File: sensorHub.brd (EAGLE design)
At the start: 160 x 100 mm, 11 parts

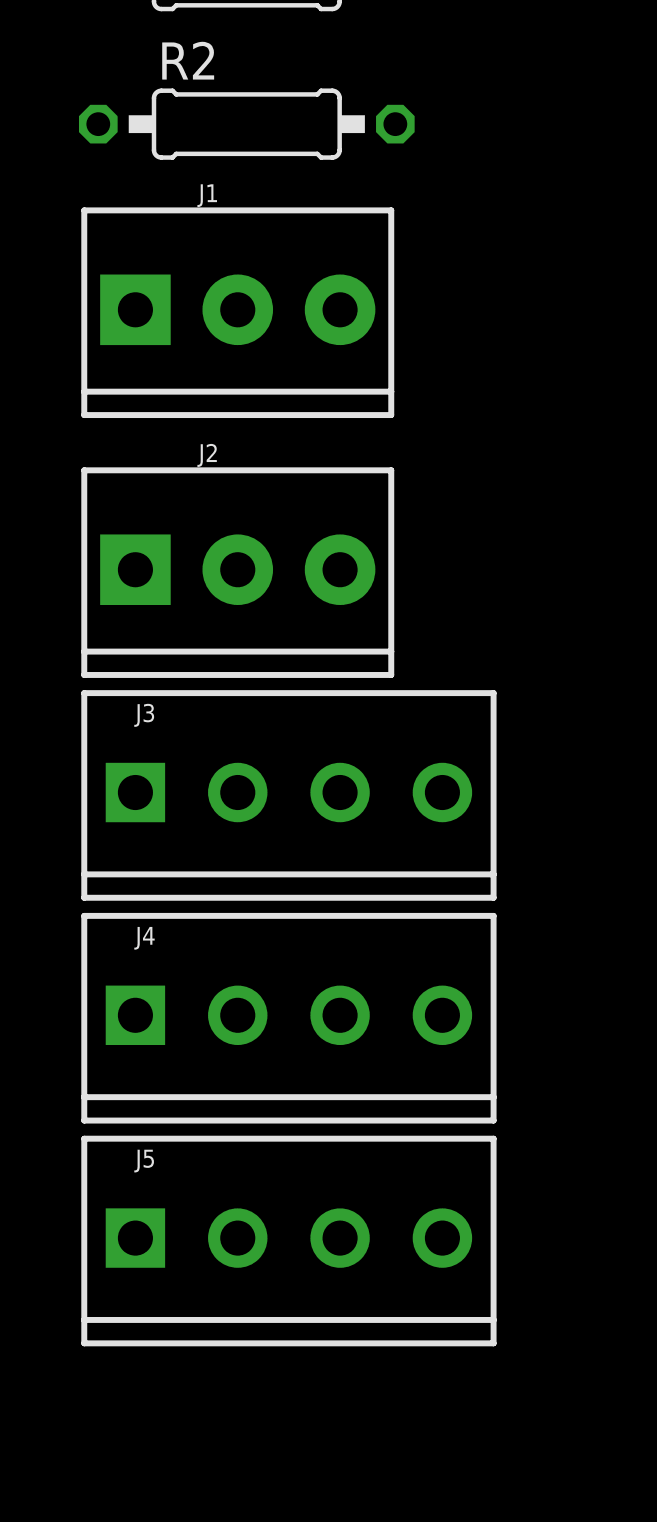
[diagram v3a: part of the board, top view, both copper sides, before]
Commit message: Completes connections in the schematic
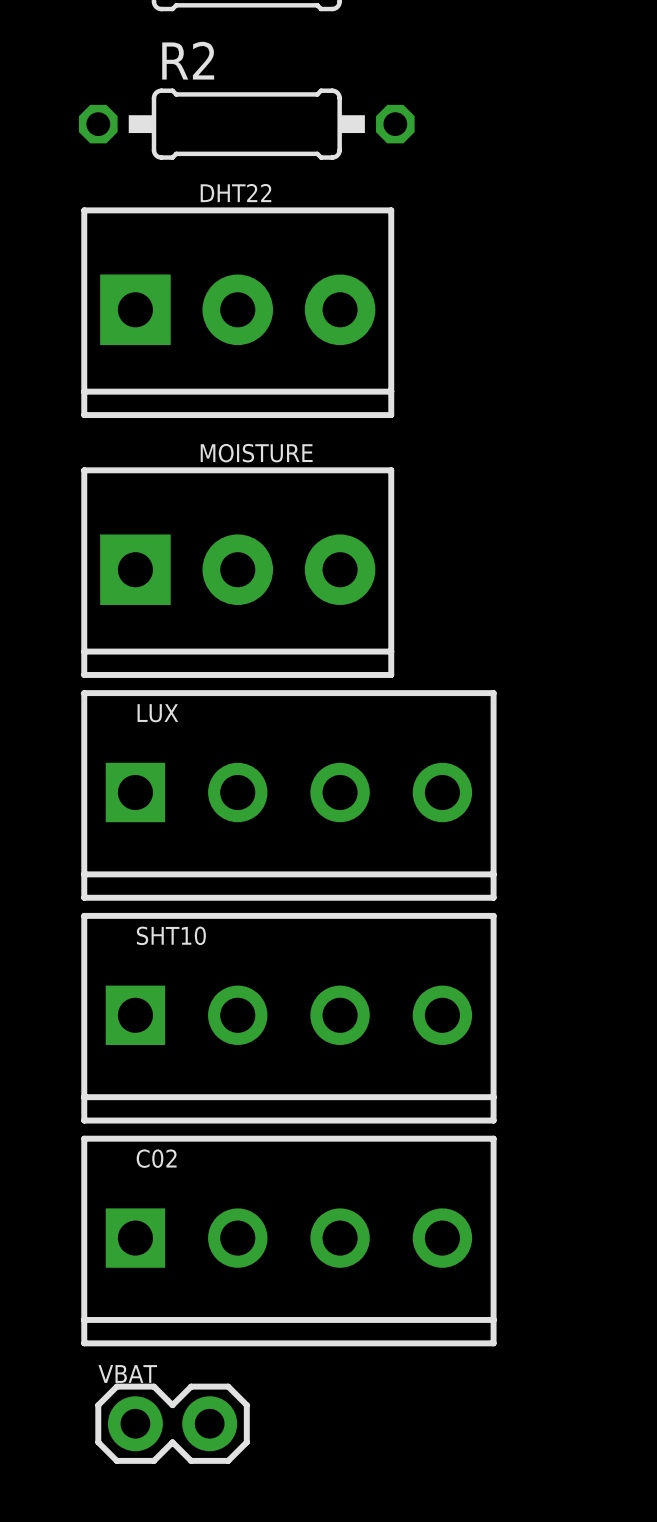
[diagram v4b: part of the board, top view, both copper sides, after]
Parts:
- added VBAT: (no value), SparkFun-Connectors:1X02
- R1, R2: value (none) -> 10k
- renumbered J1 to DHT22, J2 to MOISTURE, J3 to LUX, J4 to SHT10, J5 to C02
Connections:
- removed net OUT+: VR1.OUT+
- removed net OUT-: VR1.OUT-
- removed net VIN+: VR1.VIN+
- removed net VIN-: VR1.VIN-
- new net 3V: DHT22.1, JP1.3, JP1.4, LUX.1, MOISTURE.1, R1.1, R2.1, SHT10.1
- new net 5V: C02.2, VR1.OUT+
- new net A2: JP1.13, JP1.14, MOISTURE.2
- new net D5: DHT22.2, JP2.17, JP2.18
- new net N$1: JP1.1, JP1.2
- new net N$10: JP1.19, JP1.20
- new net N$11: JP1.21, JP1.22
- new net N$12: JP1.23, JP1.24
- new net N$13: JP1.25, JP1.26
- new net N$16: JP1.31, JP1.32
- new net N$17: JP2.1, JP2.2
- new net N$18: JP2.3, JP2.4
- new net N$19: JP2.5, JP2.6
- new net N$20: JP2.7, JP2.8
- new net N$21: JP2.10, JP2.9
- new net N$22: JP2.11, JP2.12
- new net N$23: JP2.13, JP2.14
- new net N$24: JP2.15, JP2.16
- new net N$27: VBAT.1, VBAT.2, VR1.VIN+
- new net N$3: JP1.5, JP1.6
- new net N$5: JP1.10, JP1.9
- new net N$6: JP1.11, JP1.12
- new net N$8: JP1.15, JP1.16
- new net N$9: JP1.17, JP1.18
- new net RX: C02.4, JP1.27, JP1.28
- new net SCL: JP2.19, JP2.20, LUX.3, R1.2, SHT10.3
- new net SDA: JP2.21, JP2.22, LUX.4, R2.2, SHT10.4
- new net TX: C02.3, JP1.29, JP1.30
- net GND: now also C02.1, DHT22.3, JP1.7, JP1.8, LUX.2, MOISTURE.3, SHT10.2, VR1.OUT-, VR1.VIN-

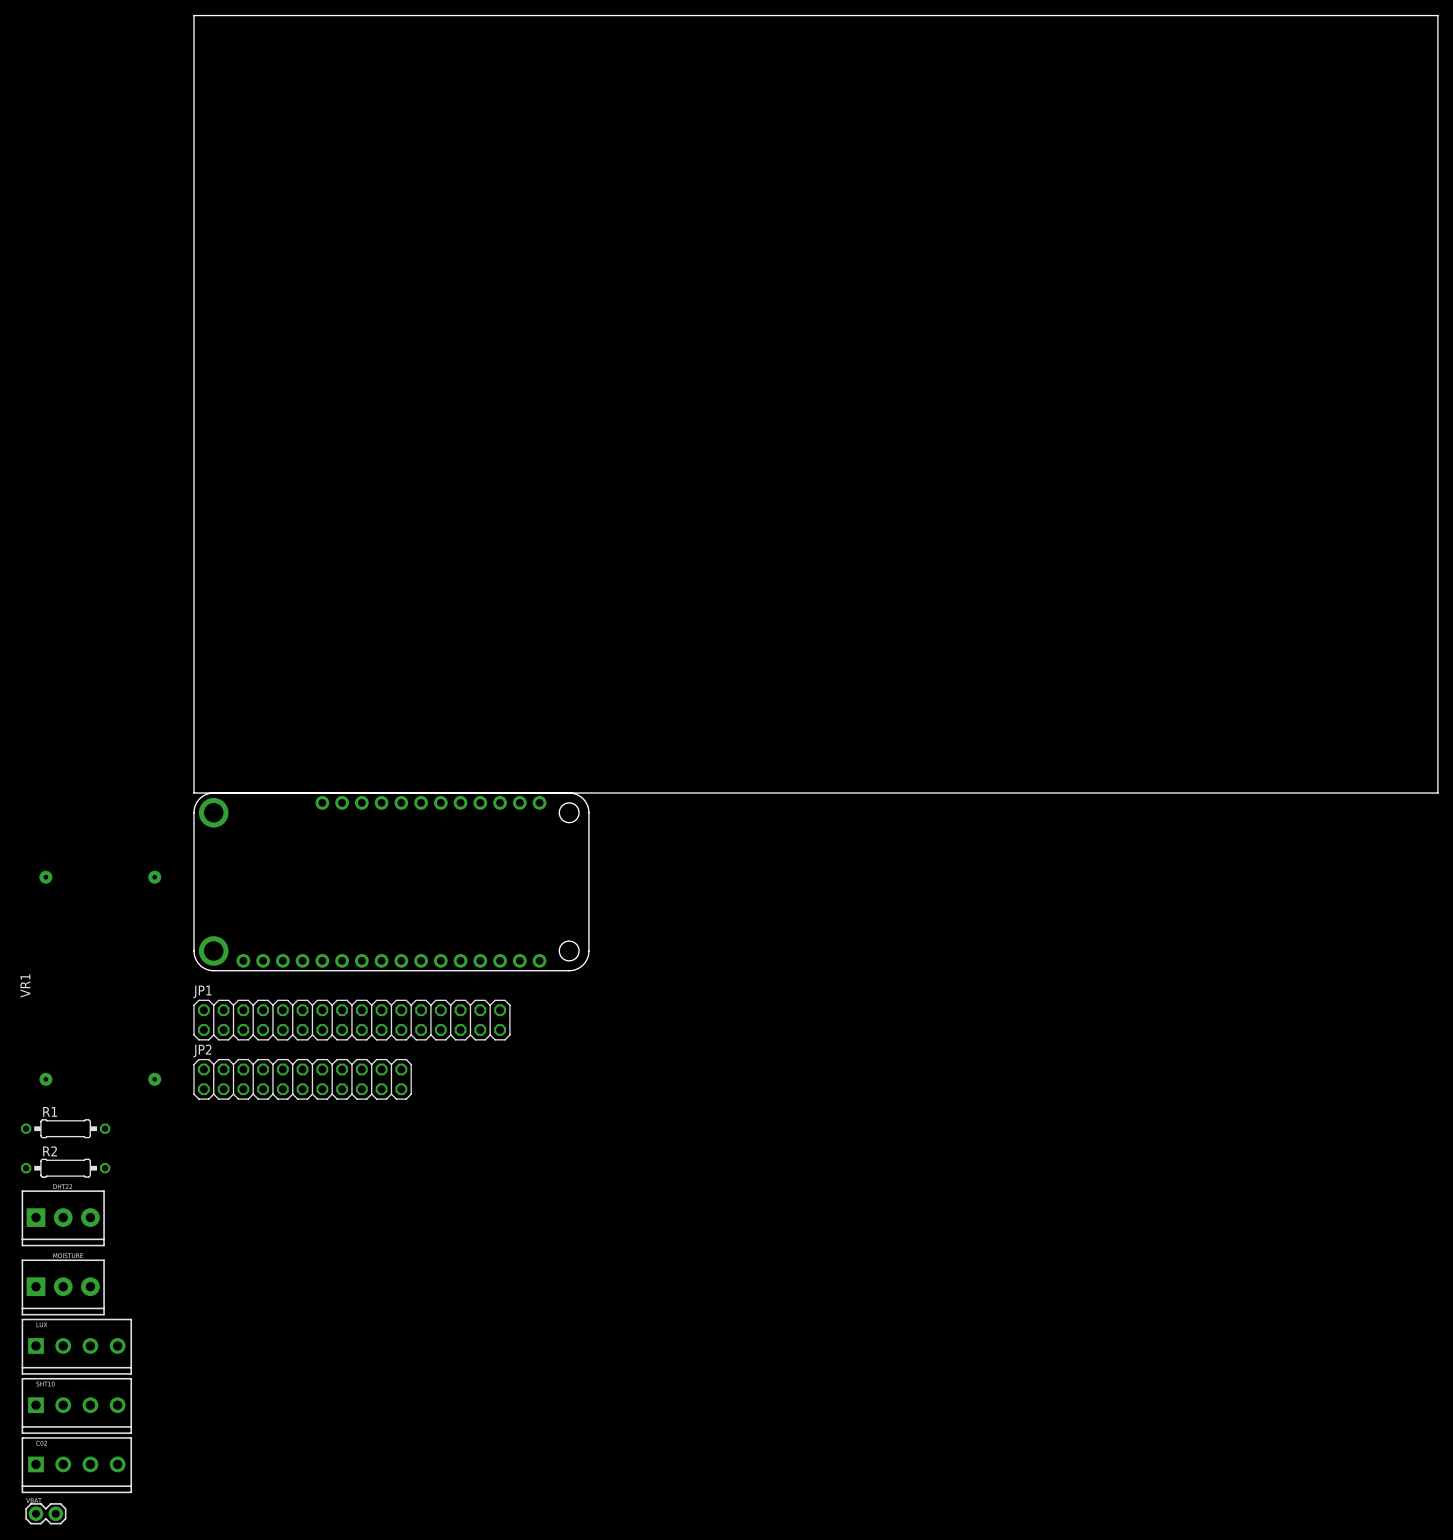
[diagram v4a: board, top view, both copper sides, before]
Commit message: Places components in pcb brd layout
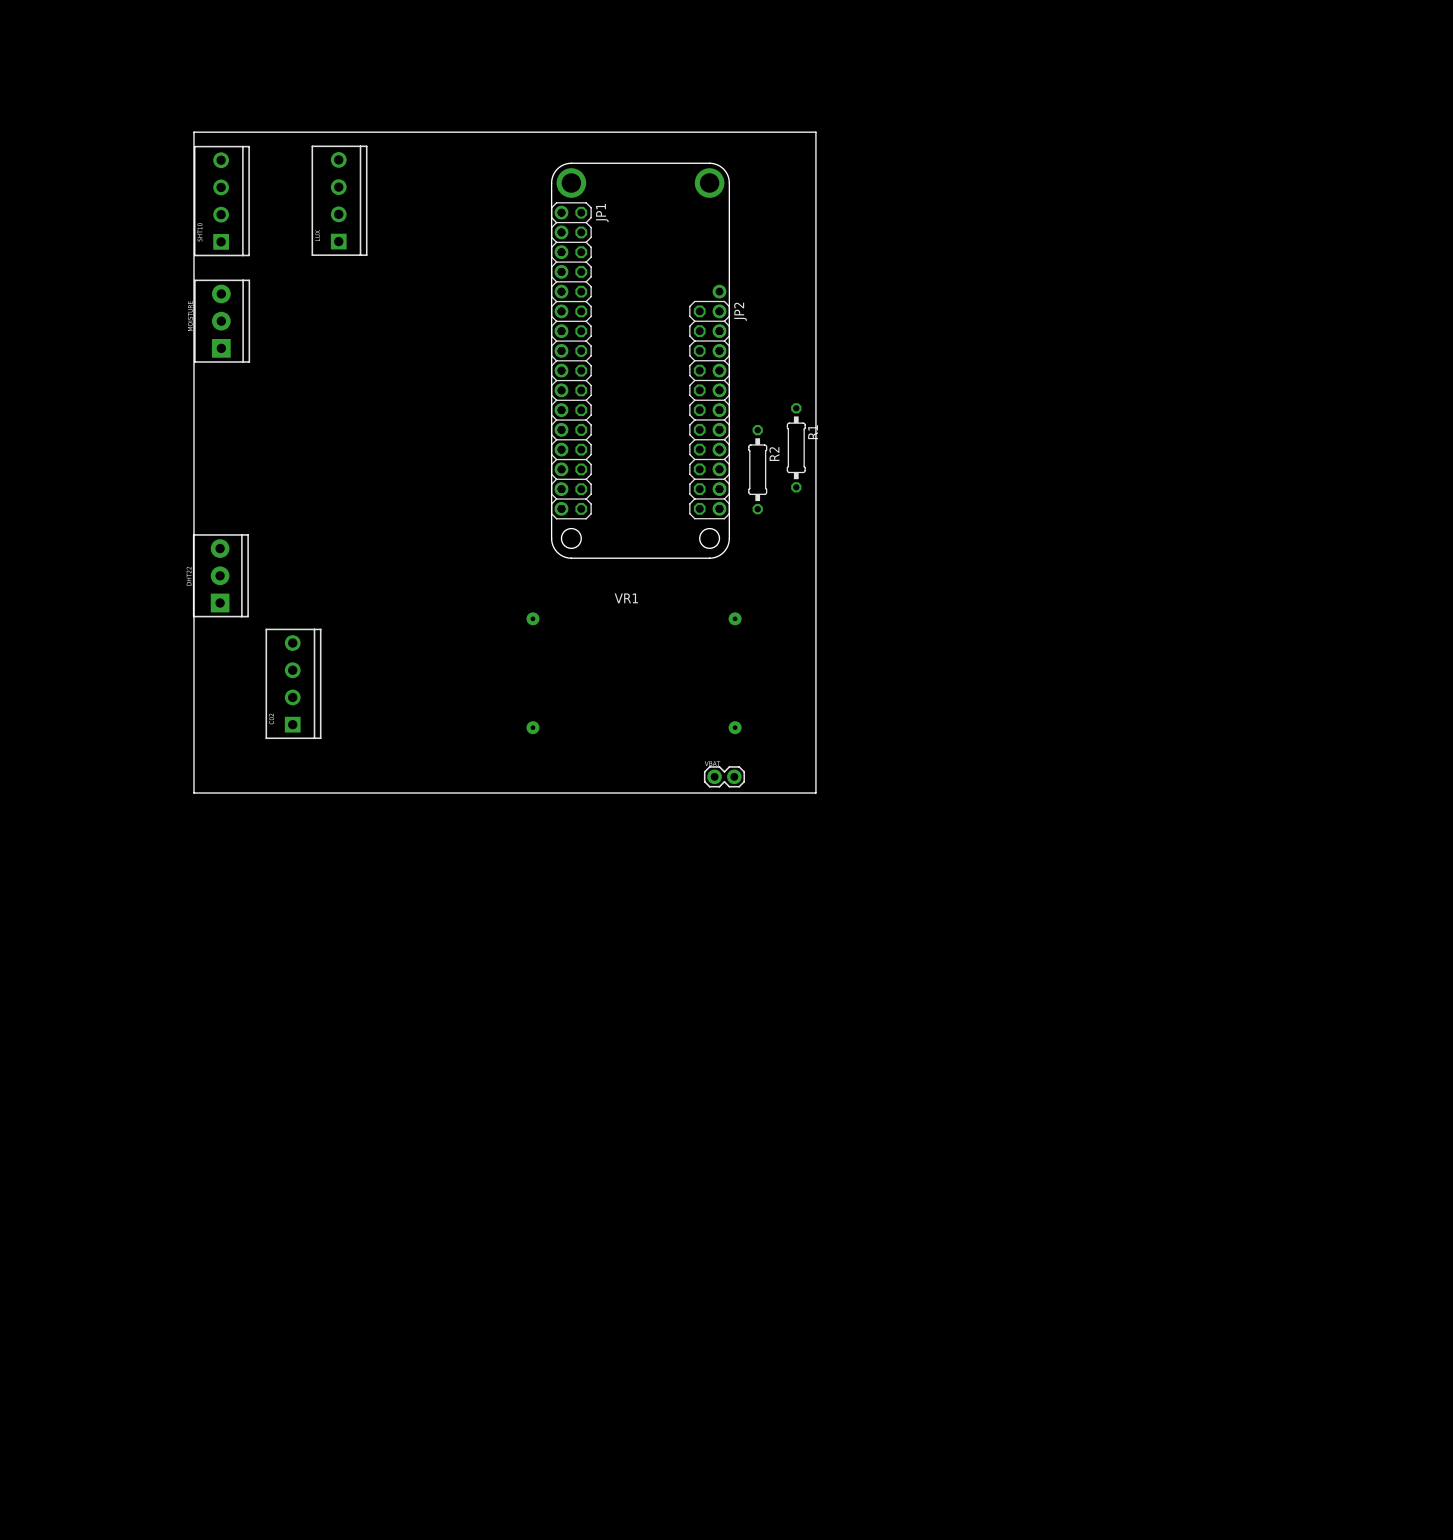
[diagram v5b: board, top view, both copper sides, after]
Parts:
- moved SHT10 151.5 mm to (3.49, 70.9), turned to 90 degrees
- moved LUX 147.3 mm to (18.6, 70.9), turned to 90 degrees
- moved VBAT 128.9 mm to (67.0, 2.08)
- moved R1 128.5 mm to (77.5, 44.4), turned to 270 degrees
- moved R2 126.5 mm to (72.5, 41.6), turned to 270 degrees
- moved MOISTURE 123.0 mm to (3.52, 57.2), turned to 90 degrees
- moved MS1 113.6 mm to (46.0, 81.0), turned to 270 degrees
- moved JP2 100.7 mm to (66.3, 49.2), turned to 270 degrees
- moved C02 100.7 mm to (12.7, 8.79), turned to 90 degrees
- moved JP1 89.4 mm to (48.5, 55.6), turned to 270 degrees
- moved VR1 86.2 mm to (43.6, 22.4), turned to 270 degrees
- moved DHT22 82.5 mm to (3.36, 24.4), turned to 90 degrees
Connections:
- net N$27 renamed VBAT
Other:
- board size 160 x 100 mm -> 80 x 85 mm

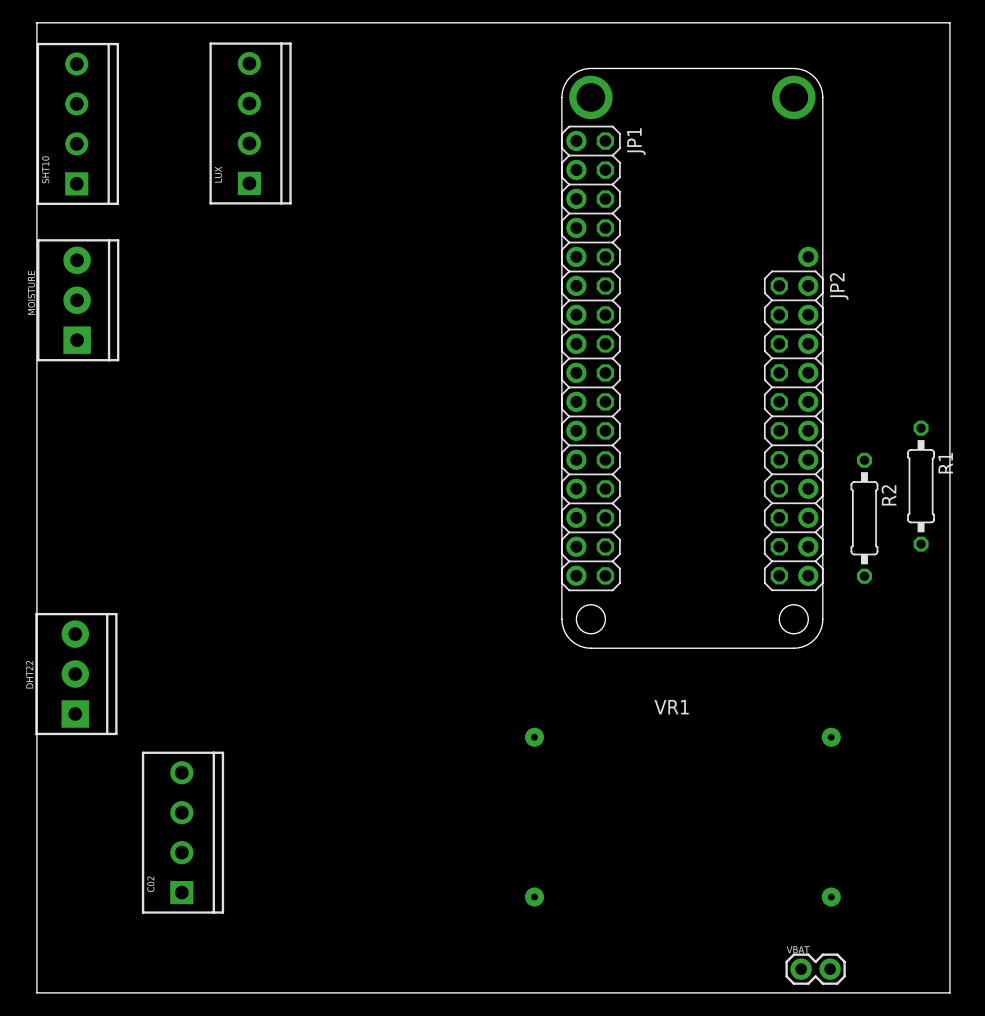
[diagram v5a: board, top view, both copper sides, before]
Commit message: Set components in place in brd file
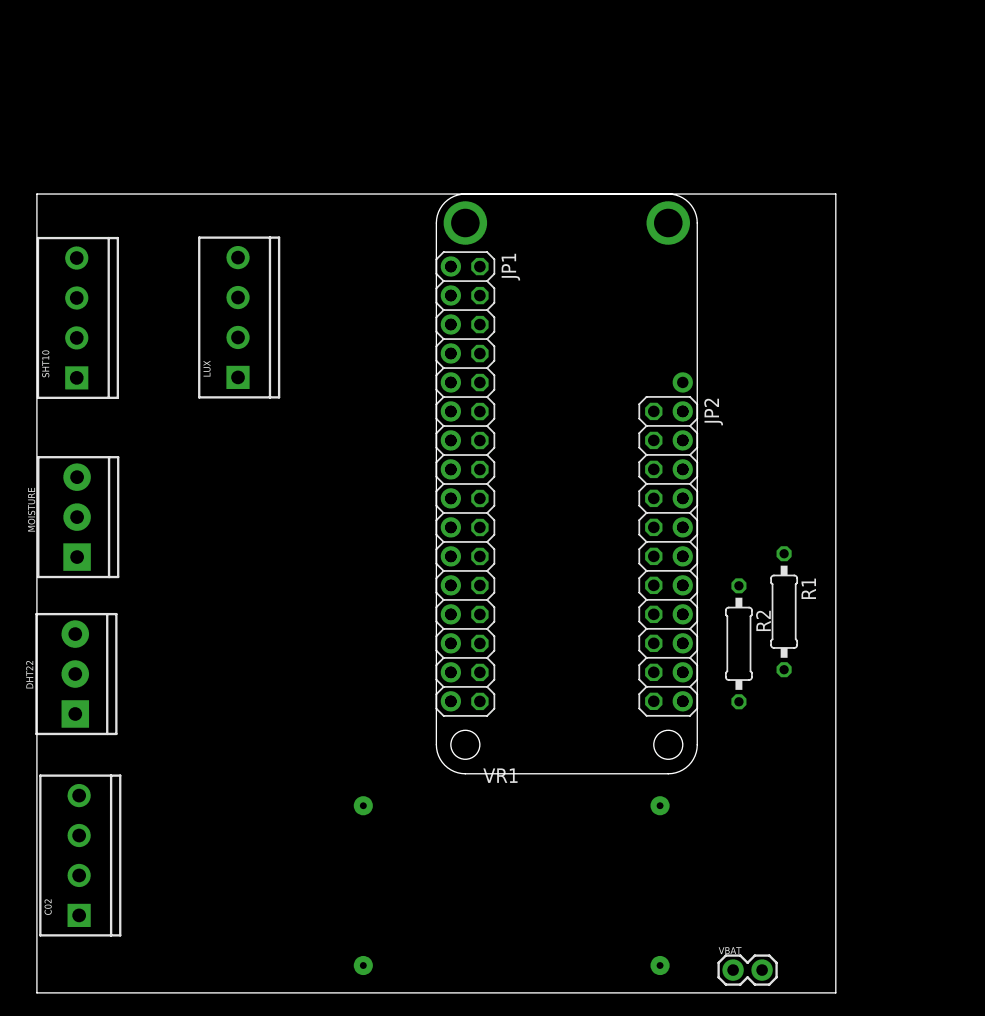
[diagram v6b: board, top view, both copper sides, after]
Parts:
- moved MOISTURE 19.0 mm to (3.52, 38.2)
- moved LUX 17.0 mm to (17.6, 53.9)
- moved SHT10 17.0 mm to (3.49, 53.9)
- moved R1 16.3 mm to (65.5, 33.4)
- moved VR1 16.2 mm to (28.6, 16.4)
- moved R2 15.6 mm to (61.5, 30.6)
- moved JP1 15.6 mm to (37.5, 44.6)
- moved MS1 15.6 mm to (35.0, 70.0)
- moved JP2 15.6 mm to (55.3, 38.2)
- moved C02 9.22 mm to (3.70, 6.79)
- moved VBAT 5.96 mm to (61.0, 2.00)
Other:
- board size 80 x 85 mm -> 70 x 70 mm
